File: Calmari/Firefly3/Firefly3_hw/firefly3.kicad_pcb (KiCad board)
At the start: 2 copper layers, 57 x 12 mm, 31 parts, among them Q1 ALS-PT19-315C, Q2 LED_RGB 5050, SW1 SWITCH

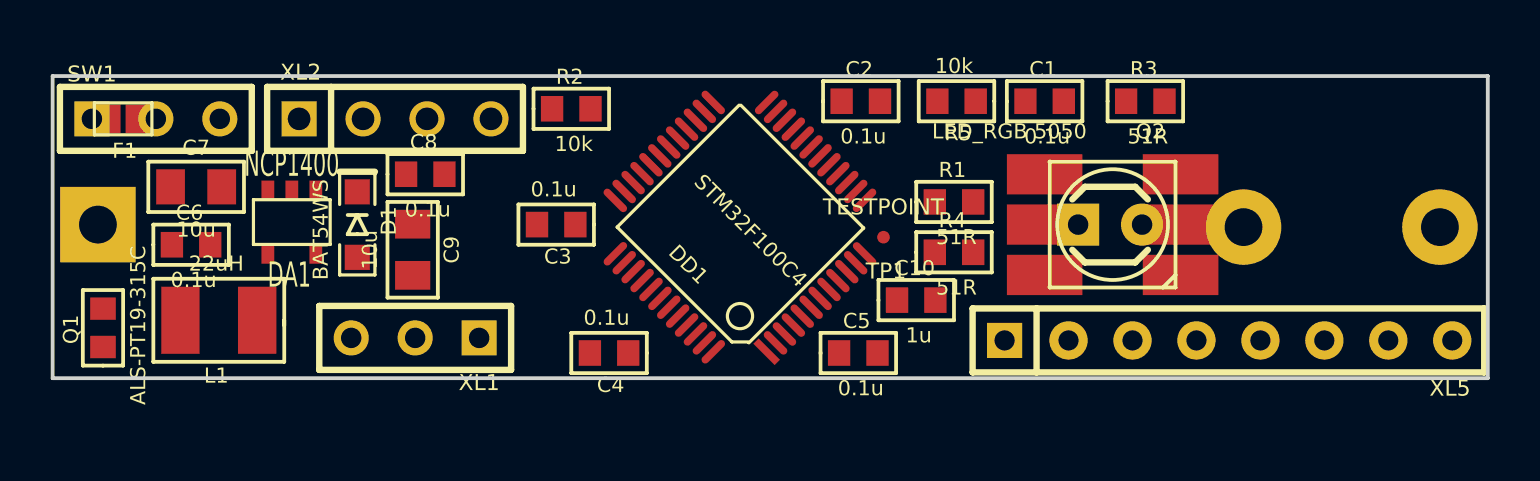
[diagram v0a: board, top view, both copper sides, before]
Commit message: Firefly3 connections updated
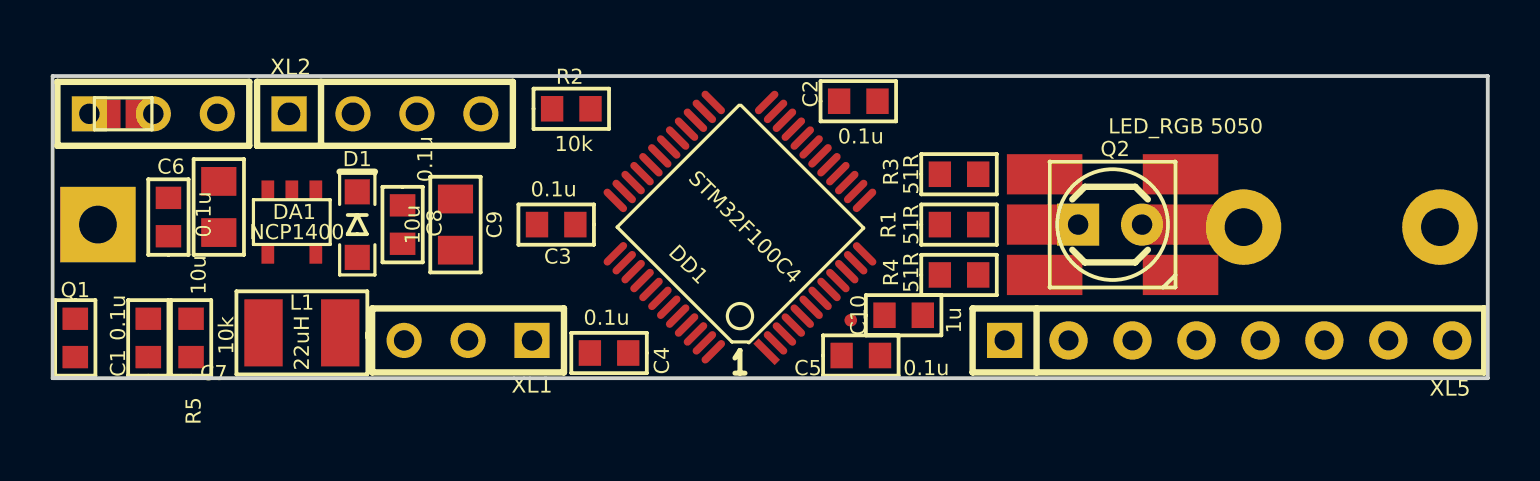
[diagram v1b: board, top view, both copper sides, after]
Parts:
- moved C1 36.8 mm to (98.8, 105.4), turned to 90 degrees
- moved R5 31.8 mm to (100.5, 105.4), turned to 90 degrees
- moved R3 7.95 mm to (131.0, 98.9)
- moved TP1 3.55 mm to (126.7, 104.7)
- moved L1 3.34 mm to (104.9, 105.2)
- moved C8 2.19 mm to (108.9, 100.9), turned to 270 degrees
- moved XL1 2.10 mm to (111.5, 105.5)
- moved C9 1.97 mm to (111.0, 100.9)
- moved C6 1.42 mm to (99.6, 100.6), turned to 90 degrees
- moved C7 1.20 mm to (101.6, 100.2), turned to 90 degrees
- moved Q1 1.17 mm to (95.9, 105.4), turned to 270 degrees
- moved R1 0.92 mm to (131.0, 100.9)
- moved R4 0.92 mm to (131.0, 102.9)
- moved C10 0.78 mm to (128.8, 104.5)
- moved XL2 0.45 mm to (108.2, 96.5)
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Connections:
- DD1 pad 11: N-000009 -> N-0000028
- DD1 pad 12: N-000006 (its old number) -> N-0000027
- DD1 pad 13: N-0000010 -> N-0000020
- DD1 pad 14: (no net) -> /5
- DD1 pad 15: (no net) -> /6
- DD1 pad 16: (no net) -> /7
- DD1 pad 17: (no net) -> /8
- DD1 pad 39: /8 -> /4
- DD1 pad 40: /7 -> (no net)
- DD1 pad 41: /6 -> (no net)
- DD1 pad 45: /5 -> (no net)
- DD1 pad 46: /4 -> (no net)
- F1 pad 1: N-0000030 (its old number) -> /BAT_IN
- R1 pad 1: N-000009 -> N-0000027
- R3 pad 1: N-000006 (its old number) -> N-0000020
- R4 pad 1: N-0000010 -> N-0000028
- SW1 pad 1: +BATT -> /BAT_IN
- SW1 pad 2: N-0000030 (its old number) -> +BATT
- XL3 pad 1: N-0000030 (its old number) -> /BAT_IN
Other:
- net class Default: clearance 0.254 -> 0.2; trace_width 0.254 -> 0.2; via_dia 0.889 -> 0.9; via_drill 0.635 -> 0.4
- net class Wide added: clearance 0.2, trace_width 0.5, via_dia 0.9, via_drill 0.4
- rule trace_clearance: 0.254 -> 0.2
- rule trace_min: 0.254 -> 0.2
- rule via_min_drill: 0.508 -> 0.4

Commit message: 
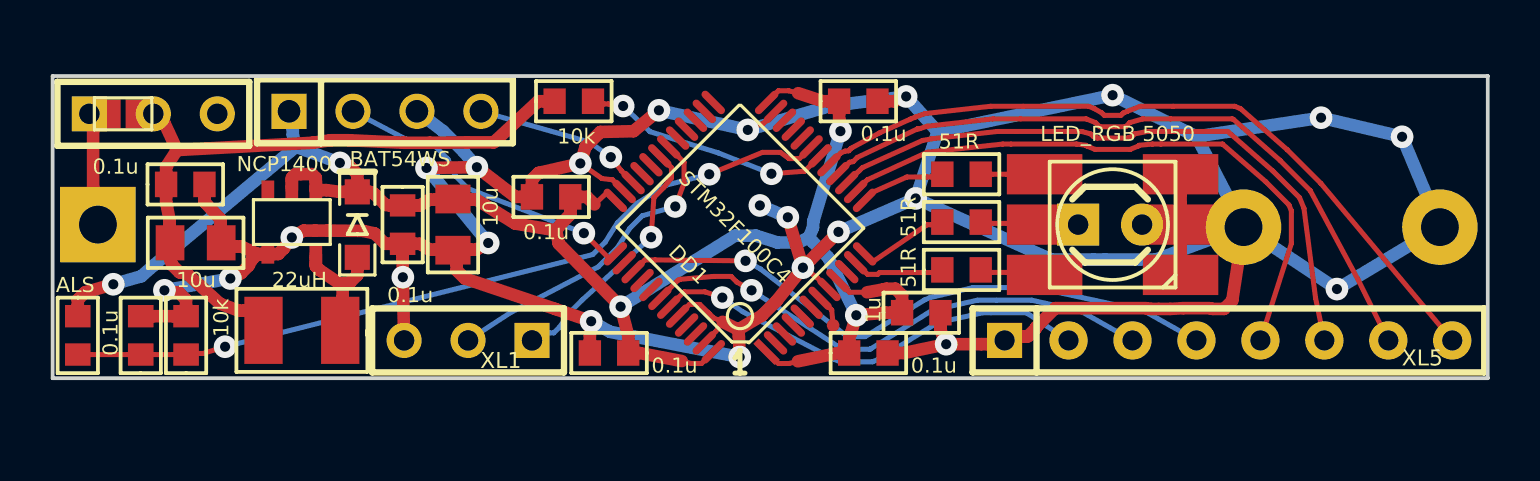
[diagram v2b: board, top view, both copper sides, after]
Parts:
- Q1: value ALS-PT19-315C -> ALS
- moved C7 1.69 mm to (100.7, 101.6), turned to 0 degrees
- moved C6 1.46 mm to (100.3, 99.3), turned to 0 degrees
- moved C3 1.12 mm to (114.8, 99.8)
- moved TP1 0.73 mm to (126.0, 104.9)
- moved C10 0.71 mm to (129.5, 104.4)
- moved C5 0.32 mm to (127.4, 106.0)
- moved C1 0.32 mm to (98.5, 105.3)
- moved R2 0.32 mm to (115.7, 96.0)
- moved R5 0.22 mm to (100.3, 105.3)
- moved R4 0.22 mm to (131.1, 102.7)
- moved Q1 0.14 mm to (96.0, 105.3)
- moved R1 0.14 mm to (131.1, 100.8)
- moved L1 0.10 mm to (104.9, 105.1)
- moved C9 0.10 mm to (110.9, 100.9)
- moved R3 0.10 mm to (131.1, 98.9)
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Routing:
- net GND: track 0.00 -> 173.2 mm, vias 0 -> 23
- net +3.3V: track 0.00 -> 72.9 mm, vias 0 -> 5
- net N-000007: track 0.00 -> 31.3 mm, vias 0 -> 2
- net /8: track 0.00 -> 29.6 mm
- net +BATT: track 0.00 -> 27.5 mm
- net /7: track 0.00 -> 27.3 mm
- net /6: track 0.00 -> 25.4 mm
- net /4: track 0.00 -> 24.5 mm, vias 0 -> 1
- net /5: track 0.00 -> 24.3 mm
- net /3: track 0.00 -> 20.8 mm, vias 0 -> 1
- net /2: track 0.00 -> 17.6 mm, vias 0 -> 1
- net /TX: track 0.00 -> 12.7 mm, vias 0 -> 1
- net /SB_SWCLK: track 0.00 -> 12.4 mm, vias 0 -> 1
- net /RX: track 0.00 -> 10.1 mm, vias 0 -> 1
- net N-000004: track 0.00 -> 9.99 mm, vias 0 -> 2
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
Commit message: 
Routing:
- added copper zone on B.Cu, net GND
- added copper zone on F.Cu, net GND
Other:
- rule pad_to_mask_clearance: 0 -> 0.1
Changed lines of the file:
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@@
   (general
     (links 73)
-    (no_connects 72)
-    (area 93.92546 94.05337 152.496676 110.107393)
+    (no_connects 0)
+    (area 94.478863 94.802999 152.496676 107.100001)
     (thickness 1.6)
     (drawings 8)
@@
   (page A3)
   (layers
-    (15 F.Cu signal hide)
-    (0 B.Cu signal hide)
+    (15 F.Cu signal)
+    (0 B.Cu signal)
     (16 B.Adhes user)
     (17 F.Adhes user)
@@
     (last_trace_width 0.2)
     (trace_clearance 0.2)
-    (zone_clearance 0.508)
+    (zone_clearance 0.3)
     (zone_45_only no)
     (trace_min 0.2)
@@
     (pad_size 1 1)
     (pad_drill 0.6)
-    (pad_to_mask_clearance 0)
+    (pad_to_mask_clearance 0.1)
     (aux_axis_origin 0 0)
     (visible_elements 7FFFFFFF)
     (pcbplotparams
-      (layerselection 3178497)
+      (layerselection 283148289)
       (usegerberextensions true)
       (excludeedgelayer true)
@@
       (outputformat 1)
       (mirror false)
-      (drillshape 1)
+      (drillshape 0)
       (scaleselection 1)
-      (outputdirectory ""))
+      (outputdirectory Gerber))
   )
   (net 0 "")
@@
   (segment (start 132.2065 102.7995) (end 132.3065 102.7995) (width 0.2) (layer F.Cu) (net 25))
   (segment (start 131.862 102.7) (end 132.2065 102.7995) (width 0.2) (layer F.Cu) (net 25))
+  (zone (net 16) (net_name GND) (layer F.Cu) (hatch edge 0.508)
+    (connect_pads (clearance 0.3))
+    (min_thickness 0.254)
+    (fill (arc_segments 16) (thermal_gap 0.3) (thermal_bridge_width 0.3))
+    (polygon
+      (pts
+        (xy 152 107) (xy 95 107) (xy 95 95) (xy 152 95)
+      )
+    )
+  )
+  (zone (net 16) (net_name GND) (layer B.Cu) (hatch edge 0.508)
+    (connect_pads (clearance 0.3))
+    (min_thickness 0.254)
+    (fill (arc_segments 16) (thermal_gap 0.3) (thermal_bridge_width 0.3))
+    (polygon
+      (pts
+        (xy 152 107) (xy 95 107) (xy 95 95) (xy 152 95)
+      )
+    )
+  )
 )
